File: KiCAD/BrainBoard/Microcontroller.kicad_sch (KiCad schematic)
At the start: 17 parts, among them J2 USB4216-03-A, SW1 SW_SPDT, U6 STM32F303CCTx, Y1 NX3225SA-32.000MHZ-STD-CSR-1

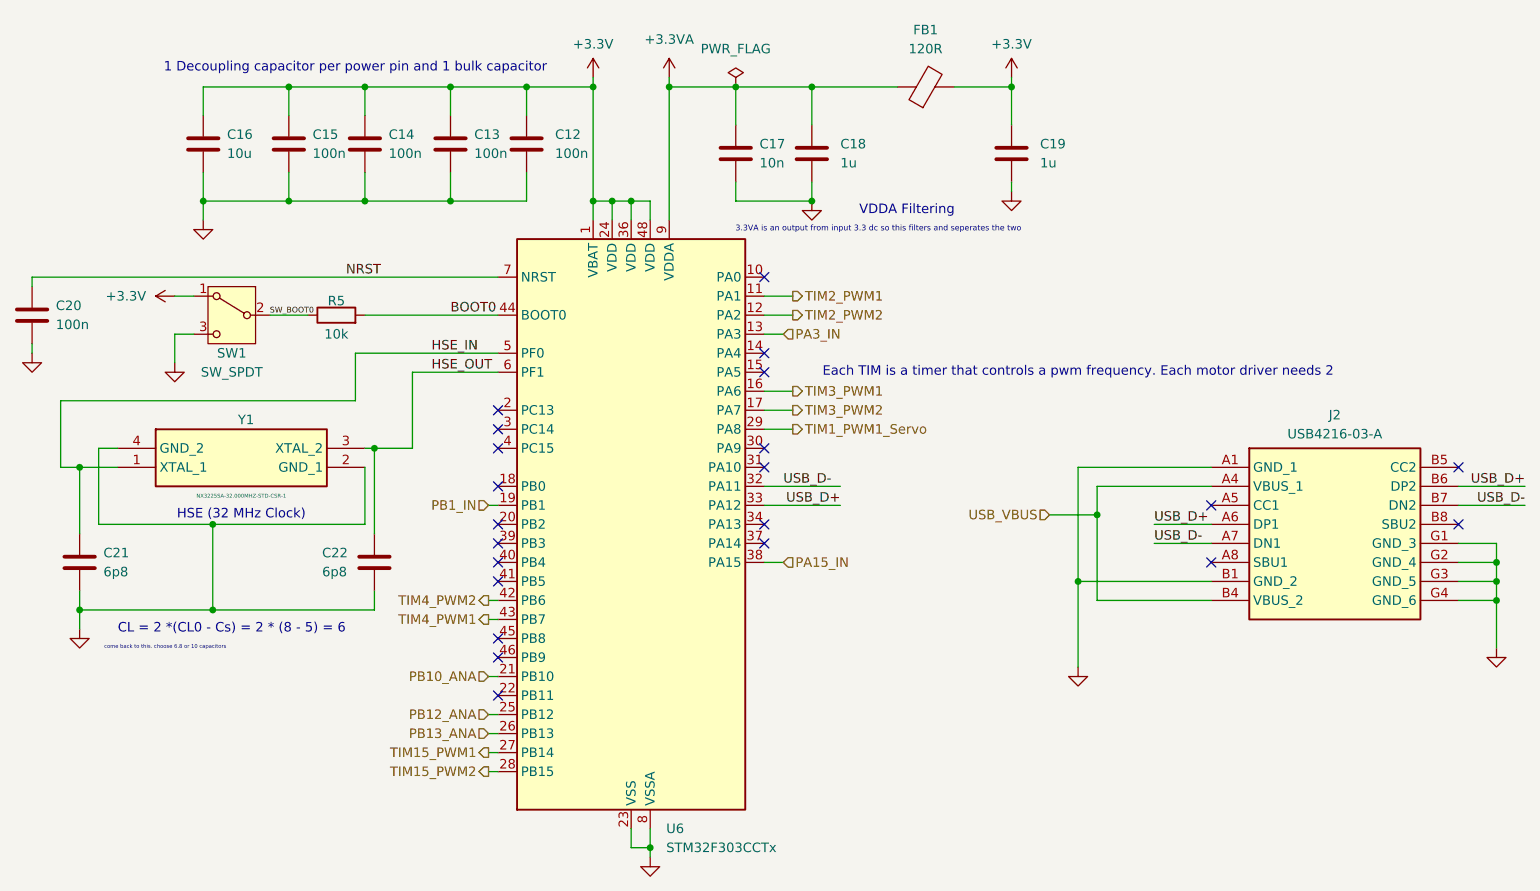
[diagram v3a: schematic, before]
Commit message: feat: added hiearchal power pins to microcontroller to avoid having global labels in hiearchal sheets
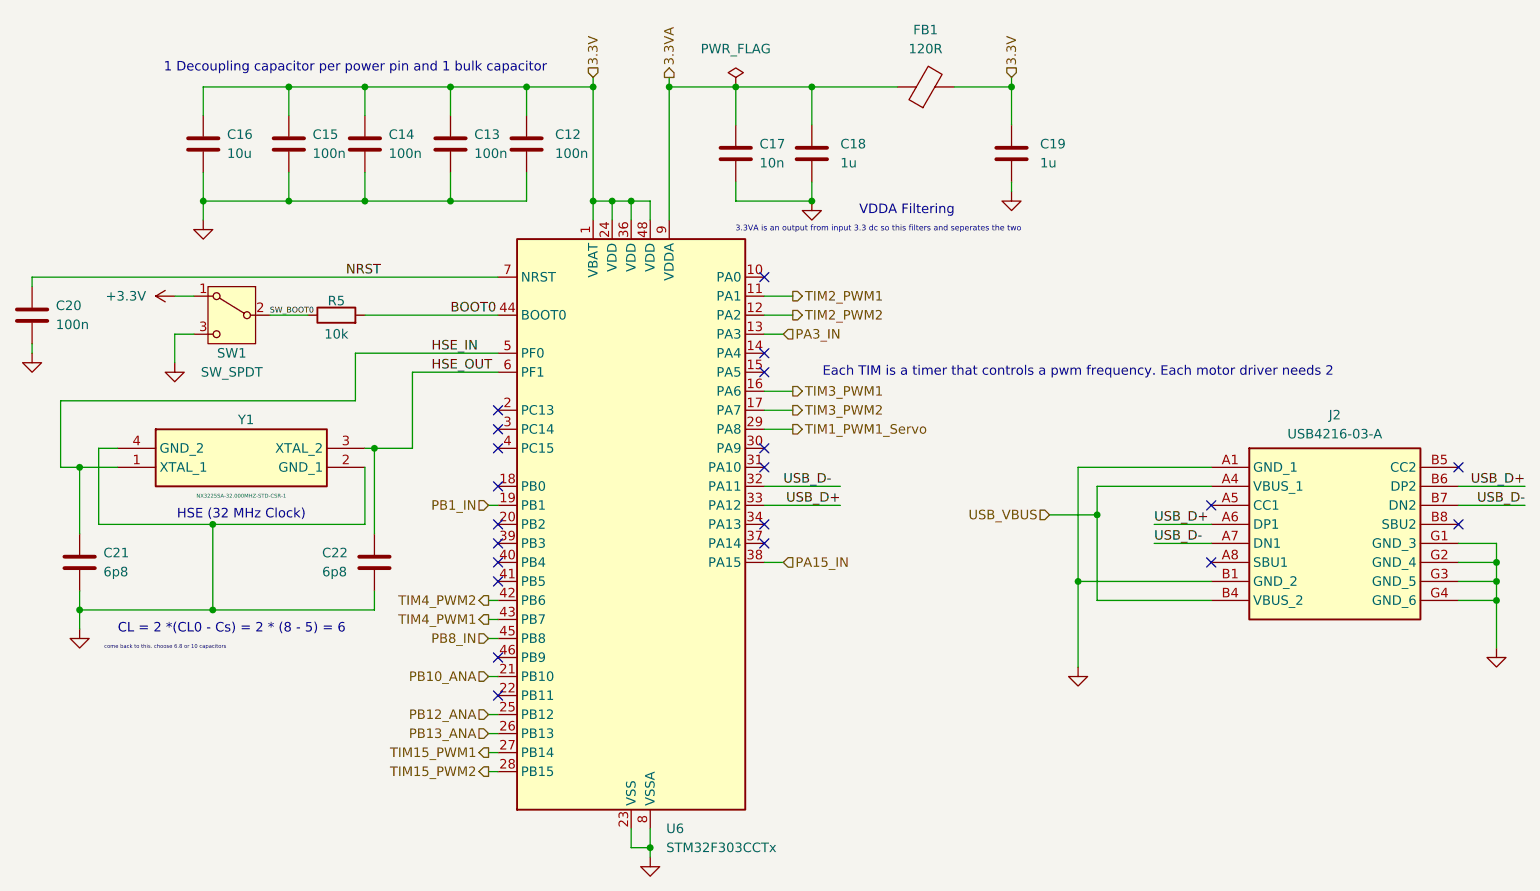
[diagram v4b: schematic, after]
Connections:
- net +3.3V: no longer C12.1, C13.1, C14.1, C15.1, C16.1, C19.1, FB1.2, U6.1 (VBAT), U6.24 (VDD), U6.36 (VDD), U6.48 (VDD)
- net PB8_IN: now reaches U6.45 (PB8)
- net +3.3VA renamed 3.3VA
- new net 3.3V: C12.1, C13.1, C14.1, C15.1, C16.1, C19.1, FB1.2, U6.1 (VBAT), U6.24 (VDD), U6.36 (VDD), U6.48 (VDD)
- no-connect marks 22 -> 21
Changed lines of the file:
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@@
 	)
 	(no_connect
-		(at 127 100.33)
-	)
-	(no_connect
 		(at 127 102.87)
 	)
@@
 	(wire
 		(pts
+			(xy 125.73 100.33) (xy 127 100.33)
+		)
+		(stroke
+			(width 0)
+			(type default)
+		)
+	)
+	(wire
+		(pts
 			(xy 149.86 25.4) (xy 149.86 26.67)
 		)
@@
 		)
 	)
+	(hierarchical_label "3.3V"
+		(shape input)
+		(at 195.58 25.4 90)
+		(effects
+			(font
+				(size 1.27 1.27)
+			)
+			(justify left)
+		)
+	)
 	(hierarchical_label "TIM3_PWM1"
 		(shape output)
@@
 		)
 	)
+	(hierarchical_label "3.3VA"
+		(shape output)
+		(at 149.86 25.4 90)
+		(effects
+			(font
+				(size 1.27 1.27)
+			)
+			(justify left)
+		)
+	)
 	(hierarchical_label "TIM1_PWM1_Servo"
 		(shape output)
@@
 		)
 	)
+	(hierarchical_label "3.3V"
+		(shape input)
+		(at 139.7 25.4 90)
+		(effects
+			(font
+				(size 1.27 1.27)
+			)
+			(justify left)
+		)
+	)
 	(hierarchical_label "PB13_ANA"
 		(shape input)
@@
 		)
 	)
+	(hierarchical_label "PB8_IN"
+		(shape input)
+		(at 125.73 100.33 180)
+		(effects
+			(font
+				(size 1.27 1.27)
+			)
+			(justify right)
+		)
+	)
 	(hierarchical_label "TIM15_PWM2"
 		(shape output)
@@
 	)
 	(symbol
-		(lib_id "power:+3.3VA")
-		(at 149.86 25.4 0)
-		(unit 1)
-		(exclude_from_sim no)
-		(in_bom yes)
-		(on_board yes)
-		(dnp no)
-		(fields_autoplaced yes)
-		(property "Reference" "#PWR018"
-			(at 149.86 29.21 0)
-			(effects
-				(font
-					(size 1.27 1.27)
-				)
-				(hide yes)
-			)
-		)
-		(property "Value" "+3.3VA"
-			(at 149.86 20.32 0)
-			(effects
-				(font
-					(size 1.27 1.27)
-				)
-			)
-		)
-		(property "Footprint" ""
-			(at 149.86 25.4 0)
-			(effects
-				(font
-					(size 1.27 1.27)
-				)
-				(hide yes)
-			)
-		)
-		(property "Datasheet" ""
-			(at 149.86 25.4 0)
-			(effects
-				(font
-					(size 1.27 1.27)
-				)
-				(hide yes)
-			)
-		)
-		(property "Description" "Power symbol creates a global label with name \"+3.3VA\""
-			(at 149.86 25.4 0)
-			(effects
-				(font
-					(size 1.27 1.27)
-				)
-				(hide yes)
-			)
-		)
-		(pin "1"
-		)
-		(instances
-			(project ""
-				(path "/44e391a9-9312-4881-bf0a-d93a44472e34/d2605501-e14c-4941-bf04-a3dfdbe74b6d"
-					(reference "#PWR018")
-					(unit 1)
-				)
-			)
-		)
-	)
-	(symbol
 		(lib_id "power:GND")
 		(at 87.63 44.45 0)
@@
 	)
 	(symbol
-		(lib_id "power:+3.3V")
-		(at 139.7 25.4 0)
-		(unit 1)
-		(exclude_from_sim no)
-		(in_bom yes)
-		(on_board yes)
-		(dnp no)
-		(fields_autoplaced yes)
-		(property "Reference" "#PWR016"
-			(at 139.7 29.21 0)
-			(effects
-				(font
-					(size 1.27 1.27)
-				)
-				(hide yes)
-			)
-		)
-		(property "Value" "+3.3V"
-			(at 139.7 20.955 0)
-			(effects
-				(font
-					(size 1.27 1.27)
-				)
-			)
-		)
-		(property "Footprint" ""
-			(at 139.7 25.4 0)
-			(effects
-				(font
-					(size 1.27 1.27)
-				)
-				(hide yes)
-			)
-		)
-		(property "Datasheet" ""
-			(at 139.7 25.4 0)
-			(effects
-				(font
-					(size 1.27 1.27)
-				)
-				(hide yes)
-			)
-		)
-		(property "Description" "Power symbol creates a global label with name \"+3.3V\""
-			(at 139.7 25.4 0)
-			(effects
-				(font
-					(size 1.27 1.27)
-				)
-				(hide yes)
-			)
-		)
-		(pin "1"
-		)
-		(instances
-			(project ""
-				(path "/44e391a9-9312-4881-bf0a-d93a44472e34/d2605501-e14c-4941-bf04-a3dfdbe74b6d"
-					(reference "#PWR016")
-					(unit 1)
-				)
-			)
-		)
-	)
-	(symbol
 		(lib_id "Device:R")
 		(at 105.41 57.15 90)
@@
 					(unit 1)
 				)
-			)
-		)
-	)
-	(symbol
-		(lib_id "power:+3.3V")
-		(at 195.58 25.4 0)
-		(unit 1)
-		(exclude_from_sim no)
-		(in_bom yes)
-		(on_board yes)
-		(dnp no)
-		(fields_autoplaced yes)
-		(property "Reference" "#PWR019"
-			(at 195.58 29.21 0)
-			(effects
-				(font
-					(size 1.27 1.27)
-				)
-				(hide yes)
-			)
-		)
-		(property "Value" "+3.3V"
-			(at 195.58 20.955 0)
-			(effects
-				(font
-					(size 1.27 1.27)
-				)
-			)
-		)
-		(property "Footprint" ""
-			(at 195.58 25.4 0)
-			(effects
-				(font
-					(size 1.27 1.27)
-				)
-				(hide yes)
-			)
-		)
-		(property "Datasheet" ""
-			(at 195.58 25.4 0)
-			(effects
-				(font
-					(size 1.27 1.27)
-				)
-				(hide yes)
-			)
-		)
-		(property "Description" "Power symbol creates a global label with name \"+3.3V\""
-			(at 195.58 25.4 0)
-			(effects
-				(font
-					(size 1.27 1.27)
-				)
-				(hide yes)
-			)
-		)
-		(pin "1"
-		)
-		(instances
-			(project "BrainBoard"
-				(path "/44e391a9-9312-4881-bf0a-d93a44472e34/d2605501-e14c-4941-bf04-a3dfdbe74b6d"
-					(reference "#PWR019")
-					(unit 1)
-				)

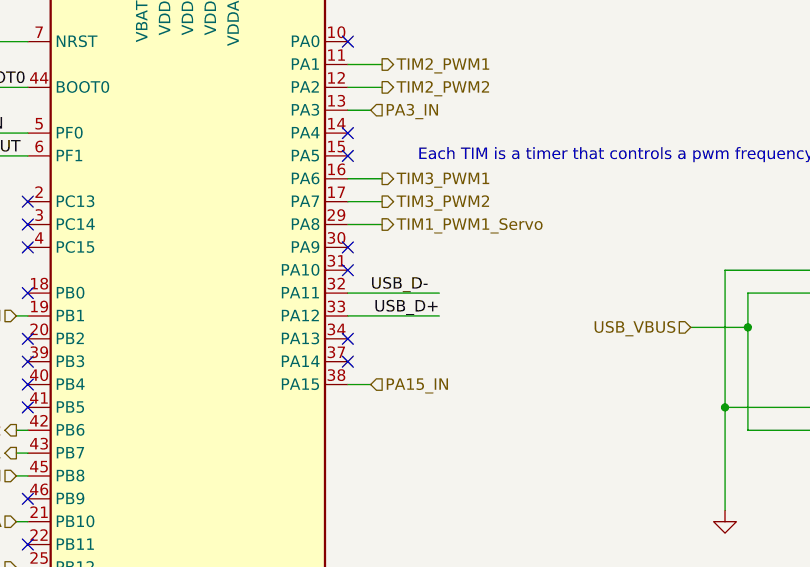
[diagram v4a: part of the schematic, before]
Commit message: feat: add +5V line
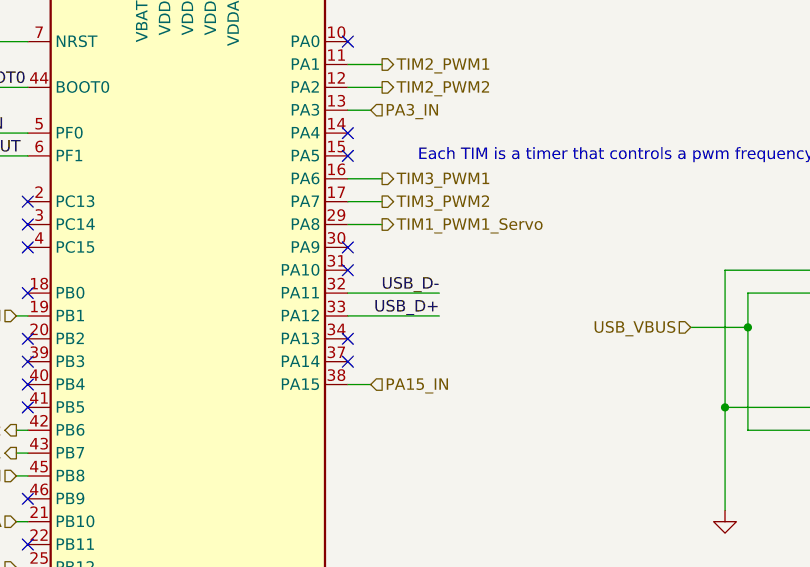
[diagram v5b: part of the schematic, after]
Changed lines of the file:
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@@
+		)
+	)
+	(label "USB_D-"
+		(at 172.72 80.01 180)
+		(effects
+			(font
+				(size 1.27 1.27)
+			)
+			(justify right bottom)
 		)
 	)
@@
 		(effects
 			(font
-				(size 1.27 1.27)
-			)
-			(justify left bottom)
-		)
-	)
-	(label "USB_D-"
-		(at 165.1 80.01 0)
-		(effects
-			(font

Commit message: Assigned most general footprints
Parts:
- C12, C13, C14, C15, C16, C17, C18, C19, C20, C21, C22: footprint (none) -> Capacitor_SMD:C_0603_1608Metric
- R5: footprint (none) -> Resistor_SMD:R_0603_1608Metric
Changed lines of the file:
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@@
 			)
 		)
-		(property "Footprint" ""
+		(property "Footprint" "Capacitor_SMD:C_0603_1608Metric"
 			(at 121.6152 38.1 0)
 			(effects
@@
 			)
 		)
-		(property "Footprint" ""
+		(property "Footprint" "Capacitor_SMD:C_0603_1608Metric"
 			(at 72.0852 93.98 0)
 			(effects
@@
 			)
 		)
-		(property "Footprint" ""
+		(property "Footprint" "Capacitor_SMD:C_0603_1608Metric"
 			(at 110.1852 38.1 0)
 			(effects
@@
 			)
 		)
-		(property "Footprint" ""
+		(property "Footprint" "Capacitor_SMD:C_0603_1608Metric"
 			(at 111.4552 93.98 0)
 			(effects
@@
 			)
 		)
-		(property "Footprint" ""
+		(property "Footprint" "Resistor_SMD:R_0603_1608Metric"
 			(at 105.41 58.928 90)
 			(effects
@@
 			)
 		)
-		(property "Footprint" ""
+		(property "Footprint" "Capacitor_SMD:C_0603_1608Metric"
 			(at 131.7752 38.1 0)
 			(effects
@@
 			)
 		)
-		(property "Footprint" ""
+		(property "Footprint" "Capacitor_SMD:C_0603_1608Metric"
 			(at 100.0252 38.1 0)
 			(effects
@@
 			)
 		)
-		(property "Footprint" ""
+		(property "Footprint" "Capacitor_SMD:C_0603_1608Metric"
 			(at 169.8752 39.37 0)
 			(effects
@@
 			)
 		)
-		(property "Footprint" ""
+		(property "Footprint" "Capacitor_SMD:C_0603_1608Metric"
 			(at 88.5952 38.1 0)
 			(effects
@@
 			)
 		)
-		(property "Footprint" ""
+		(property "Footprint" "Capacitor_SMD:C_0603_1608Metric"
 			(at 159.7152 39.37 0)
 			(effects
@@
 			)
 		)
-		(property "Footprint" ""
+		(property "Footprint" "Capacitor_SMD:C_0603_1608Metric"
 			(at 65.7352 60.96 0)
 			(effects
@@
 			)
 		)
-		(property "Footprint" ""
+		(property "Footprint" "Capacitor_SMD:C_0603_1608Metric"
 			(at 196.5452 39.37 0)
 			(effects
